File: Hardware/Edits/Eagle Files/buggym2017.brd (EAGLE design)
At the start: 88.9 x 81.3 mm, 6 parts, among them IC1-NOR 4001N, IC2-OR 4075N, IC3 BCC, IC4 L293E

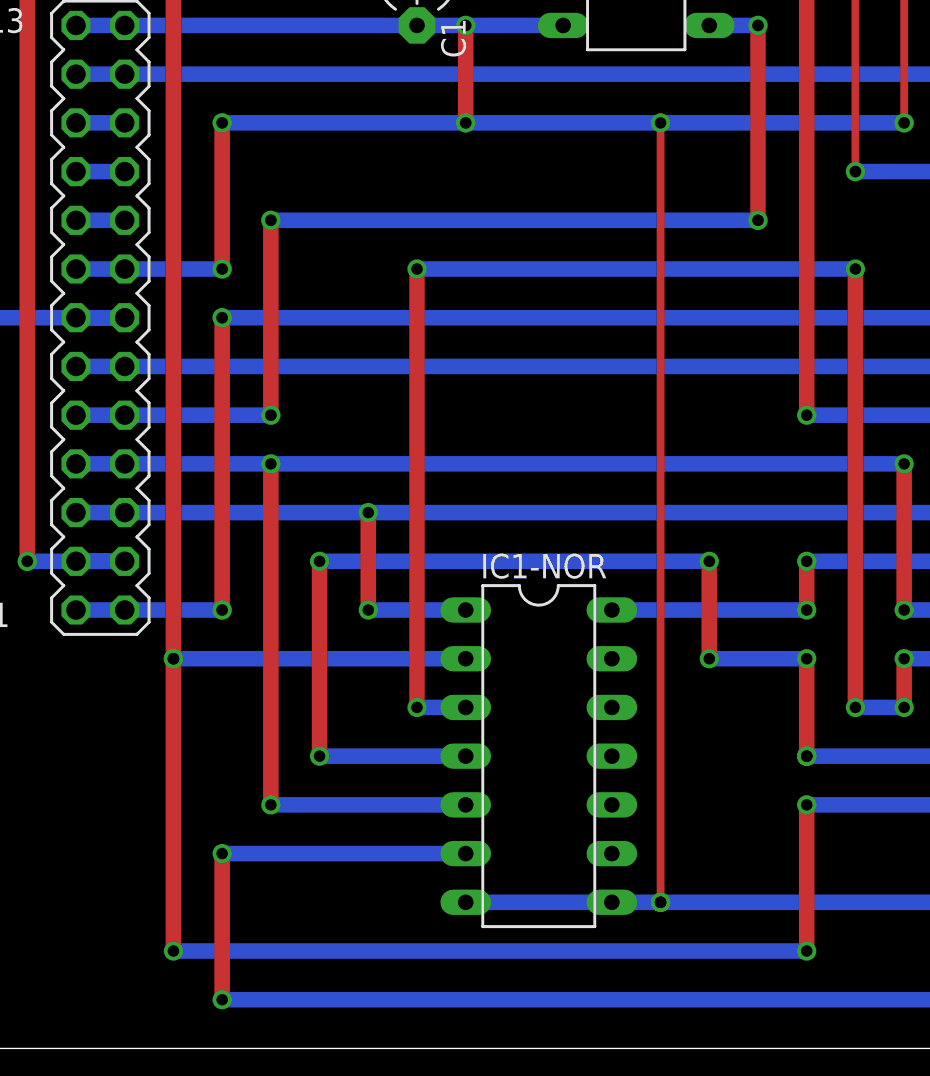
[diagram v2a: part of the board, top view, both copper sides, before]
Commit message: Eagle board more accurately reflects the final board. Thin wires represent deviations from the original given schematic with the BCC and the H-bridge.
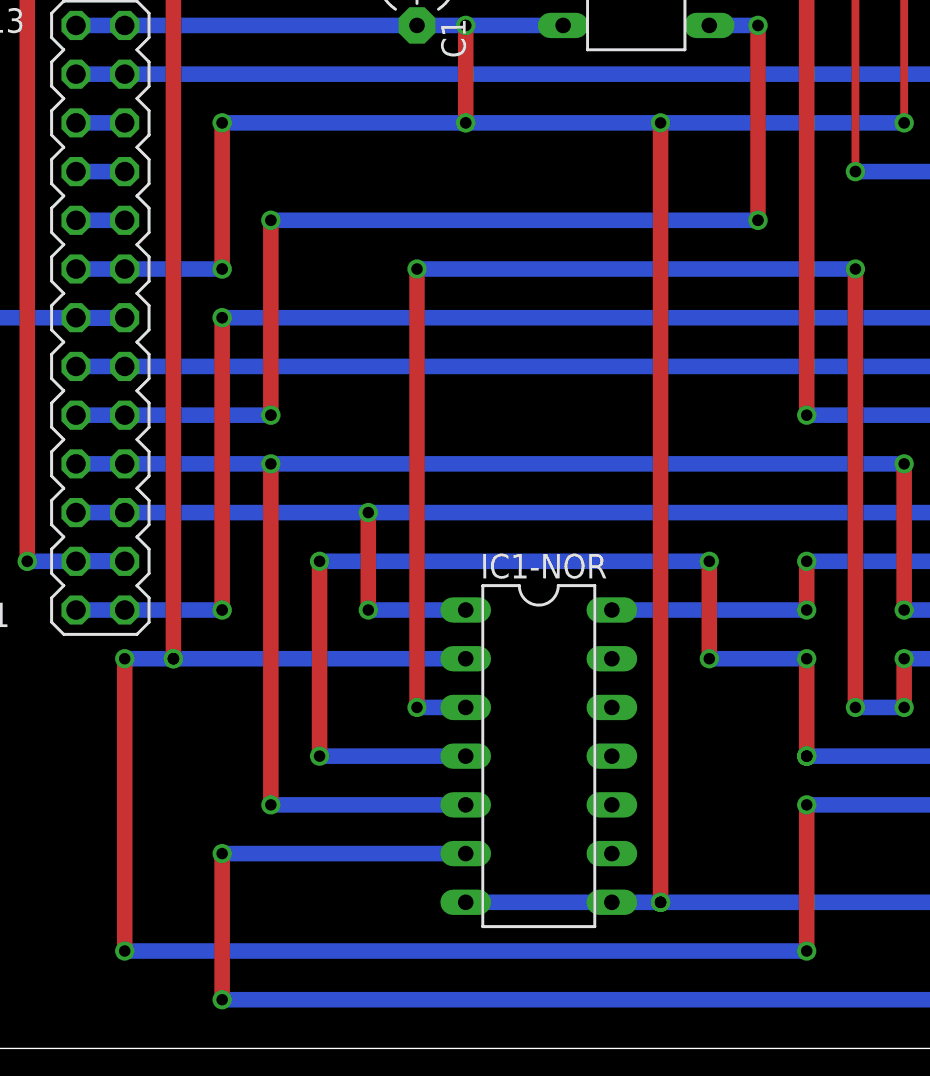
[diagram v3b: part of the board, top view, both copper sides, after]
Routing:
- net RO: track 142.2 -> 147.3 mm, vias 6 -> 7
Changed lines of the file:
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@@
 <?xml version="1.0" encoding="utf-8"?>
 <!DOCTYPE eagle SYSTEM "eagle.dtd">
-<eagle version="7.7.0">
+<eagle version="8.0.2">
 <drawing>
 <settings>
@@
 <element name="IC4" library="texas" package="DIL16" value="L293E" x="82.55" y="54.61" rot="R270">
 <attribute name="MF" value="Arrow Electronics" x="82.55" y="54.61" size="1.778" layer="27" rot="R270" display="off"/>
+<attribute name="MPN" value="L293E" x="82.55" y="54.61" size="1.778" layer="27" rot="R270" display="off"/>
 <attribute name="OC_FARNELL" value="1467711" x="82.55" y="54.61" size="1.778" layer="27" rot="R270" display="off"/>
-<attribute name="MPN" value="L293E" x="82.55" y="54.61" size="1.778" layer="27" rot="R270" display="off"/>
 <attribute name="OC_NEWARK" value="89K0732" x="82.55" y="54.61" size="1.778" layer="27" rot="R270" display="off"/>
 </element>
@@
 <via x="55.88" y="7.62" extent="1-16" drill="0.6" shape="square"/>
 <via x="55.88" y="7.62" extent="1-16" drill="0.6" shape="square"/>
-<wire x1="55.88" y1="7.62" x2="55.88" y2="48.26" width="0.4064" layer="1"/>
+<wire x1="55.88" y1="7.62" x2="55.88" y2="48.26" width="0.8128" layer="1"/>
 <via x="55.88" y="48.26" extent="1-16" drill="0.6" shape="square"/>
 <wire x1="55.88" y1="7.62" x2="78.74" y2="7.62" width="0.8128" layer="16"/>
@@
 <wire x1="45.72" y1="20.32" x2="30.48" y2="20.32" width="0.8128" layer="16"/>
 <via x="30.48" y="20.32" extent="1-16" drill="0.6" shape="square"/>
-<wire x1="30.48" y1="20.32" x2="30.48" y2="5.08" width="0.8128" layer="1"/>
-<via x="30.48" y="5.08" extent="1-16" drill="0.6" shape="square"/>
-<wire x1="30.48" y1="5.08" x2="63.5" y2="5.08" width="0.8128" layer="16"/>
 <via x="63.5" y="5.08" extent="1-16" drill="0.6" shape="square"/>
 <wire x1="63.5" y1="5.08" x2="63.5" y2="12.7" width="0.8128" layer="1"/>
 <via x="63.5" y="12.7" extent="1-16" drill="0.6" shape="square"/>
 <wire x1="63.5" y1="12.7" x2="78.74" y2="12.7" width="0.8128" layer="16"/>
+<wire x1="30.48" y1="20.32" x2="27.94" y2="20.32" width="0.8128" layer="16"/>
+<via x="27.94" y="20.32" extent="1-16" drill="0.6" shape="square"/>
+<wire x1="27.94" y1="20.32" x2="27.94" y2="5.08" width="0.8128" layer="1"/>
+<via x="27.94" y="5.08" extent="1-16" drill="0.6" shape="square"/>
+<wire x1="27.94" y1="5.08" x2="63.5" y2="5.08" width="0.8128" layer="16"/>
 </signal>
 <signal name="R_EYE">
